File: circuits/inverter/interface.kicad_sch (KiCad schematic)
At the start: 10 parts

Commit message: adds pin headers for display options
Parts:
- added C? (x2): 100n, symbol OSSI_standard_components:Capacitor
- added C?: 10u, symbol OSSI_standard_components:Capacitor
- added TP? (x2): Testpoint, symbol OSSI_standard_components:Testpoint
- added X?: TFT_CON, symbol pin_headers:header_1x08
- added X?: OLED_CON, symbol pin_headers:header_1x04
- H?: Color C -> Red
- H?: Color C -> Green
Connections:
- net +3V3: now also C?.1, C?.2, X?.1, X?.2
- net GND: now also C?.1, C?.1, C?.2, X?.1, X?.2
- net UART_RX: now also TP?.1
- net UART_TX: now also TP?.1
- net at R?.1, U?.16 (+3V3): now also C?.2
- net TFT_Data_~{Command}: now reaches U?.23 (D5_GPIO14_HSCLK)
- net TFT_Data_~{Command}: now also X?.5
- net TFT_BL: now reaches U?.4 (GPIO10_SDD3)
- net TFT_BL: now also X?.8
- net TFT_~{RESET}: now reaches U?.5 (GPIO9_SDD2)
- net TFT_~{RESET}: now also X?.4
- net TFT_MOSI: now reaches U?.6 (GPIO8_SDD1_MOSI)
- net TFT_MOSI: now also X?.6
- net TFT_~{CS}: now reaches U?.7 (GPIO_11_SDCMD_CS)
- net TFT_~{CS}: now also X?.3
- net TFT_SCLK: now reaches U?.9 (GPIO6_SDCLK_SCLK)
- net TFT_SCLK: now also X?.7
- net Node_SCL renamed OLED_SCL
- net OLED_SCL: now also X?.3
- net Node_SDA renamed OLED_SDA
- net OLED_SDA: now also X?.4
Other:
- note added: "Display Options"
- note added: "I²C OLED"
- note added: "Pin-Out needs to be checked against the actual OLED. ⚠ Pins are sometimes swapped depending on OLED supplier."
- note added: "SPI TFT"
- note added: "Test points to connect *isolated* UART interface."
- title: (none) -> Interface, Display, LED Circuit
- moved on the sheet: H?, Q?, R?

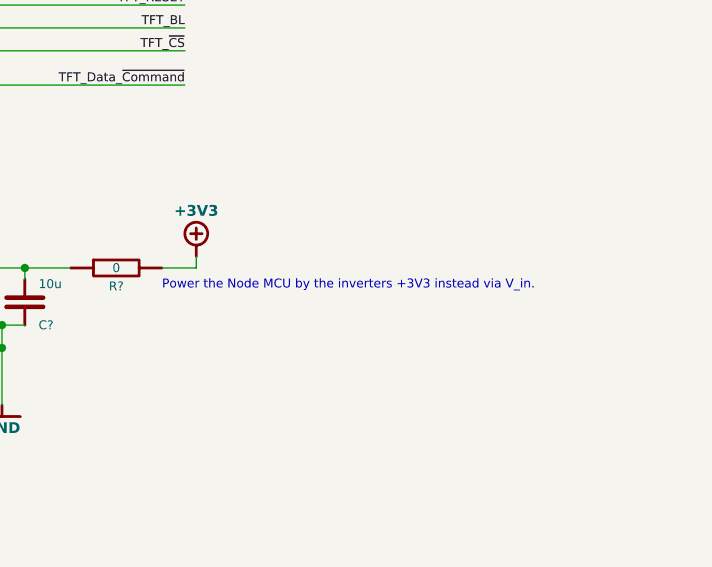
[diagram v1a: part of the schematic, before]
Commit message: converts the project to Kicad 7
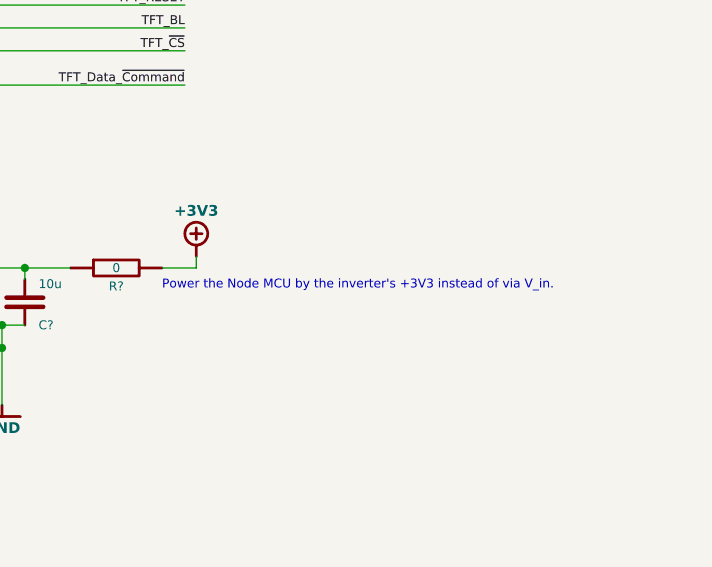
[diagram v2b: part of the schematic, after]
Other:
- note added: "Power the Node MCU by the inverter's +3V3 instead of via V_in."
- note removed: "Power the Node MCU by the inverters +3V3 instead via V_in."
